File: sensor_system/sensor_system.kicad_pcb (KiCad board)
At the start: 2 copper layers, 49 parts, among them J2 Solar_panels, Q1 SBC817, Q2 MJD45H11, SW1 SW_DPDT_x2, U1 TLC555xD, U2 XC6206PxxxMR, U3 MCP73833, U4 module_bme280_alt, U5 ESP32-DEVKIT-V1, U7 TPS63002

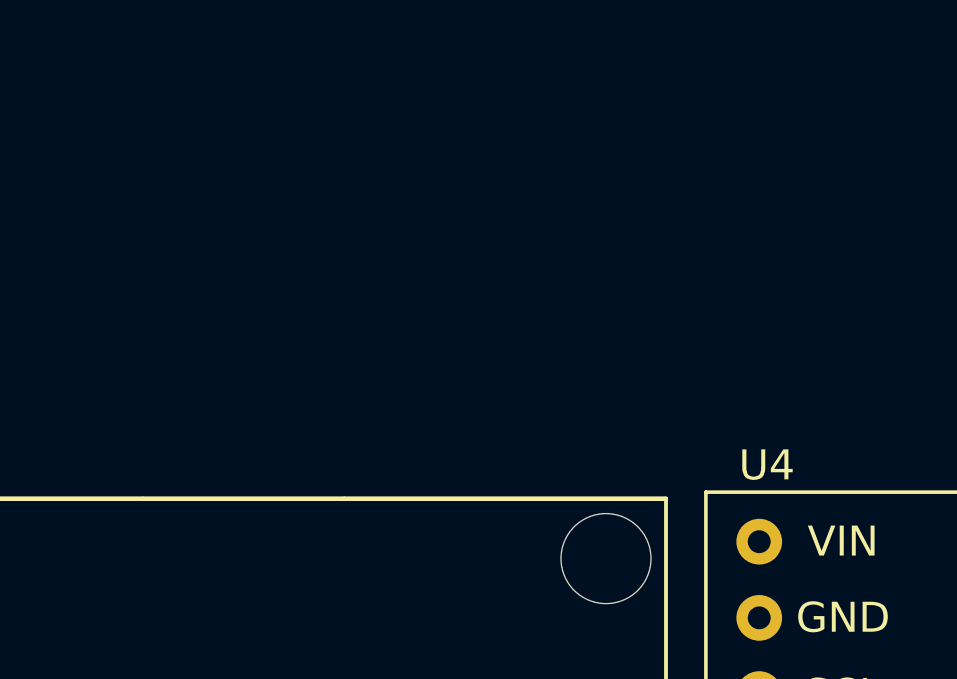
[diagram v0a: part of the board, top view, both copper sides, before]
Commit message: Izveidots footprint magnetiskajam konetoram
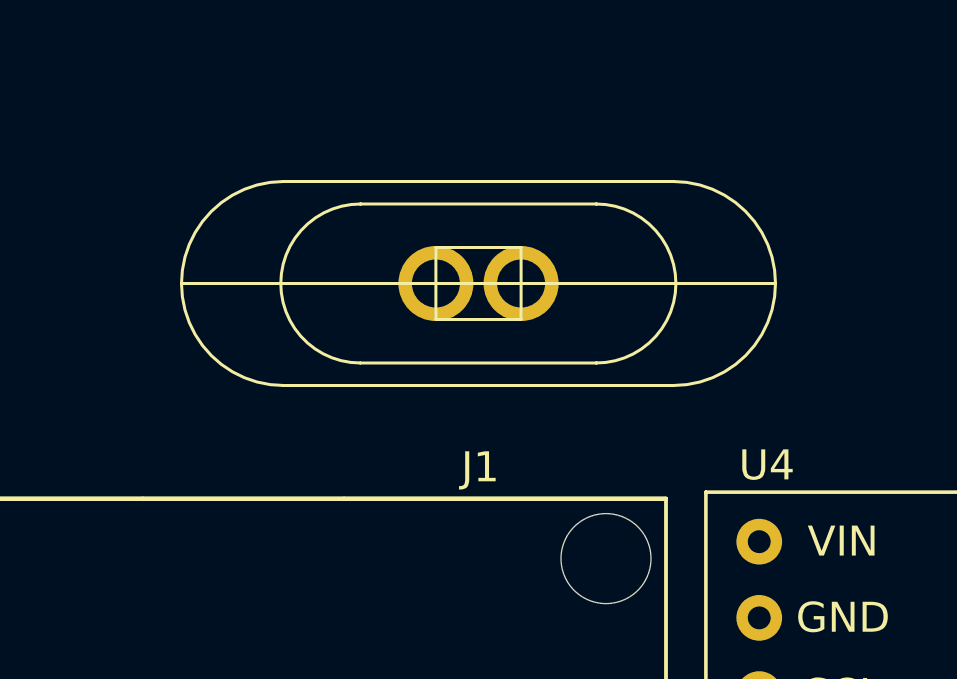
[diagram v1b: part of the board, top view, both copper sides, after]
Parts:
- added J1: Magnetic connector, Magnetic connector:Magnetic connector, F.Cu at (53.0, 25.1)
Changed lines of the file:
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@@
     )
+  )
+  (footprint "Magnetic connector:Magnetic connector" (layer "F.Cu")
+    (at 53.02 25.1)
+    (property "Sheetfile" "power_supply.kicad_sch")
+    (property "Sheetname" "power_supply")
+    (property "ki_description" "Generic screw terminal, single row, 01x02, script generated (kicad-library-utils/schlib/autogen/connector/)")
+    (property "ki_keywords" "screw terminal")
+    (attr smd)
+    (fp_text reference "J1" (at 0.06 6.13 unlocked) (layer "F.SilkS")
+        (effects (font (size 1 1) (thickness 0.1)))
+    )
+    (fp_text value "Magnetic connector" (at 0.16 4.46 unlocked) (layer "F.Fab")
+        (effects (font (size 1 1) (thickness 0.15)))
+    )
+    (fp_line (start -6.5 -3.4) (end 6.5 -3.4)
+      (stroke (width 0.1) (type default)) (layer "F.SilkS"))
+    (fp_line (start -6.5 3.4) (end 6.5 3.4)
+      (stroke (width 0.1) (type default)) (layer "F.SilkS"))
+    (fp_line (start -3.94 -2.65) (end 3.94 -2.65)
+      (stroke (width 0.1) (type default)) (layer "F.SilkS"))
+    (fp_line (start -3.94 2.65) (end 3.94 2.65)
+      (stroke (width 0.1) (type default)) (layer "F.SilkS"))
+    (fp_line (start -1.42 -1.2) (end 1.42 -1.2)
+      (stroke (width 0.1) (type default)) (layer "F.SilkS"))
+    (fp_line (start -1.42 0) (end 1.42 0)
+      (stroke (width 0.1) (type default)) (layer "F.SilkS"))
+    (fp_line (start -1.42 1.2) (end -1.42 -1.2)
+      (stroke (width 0.1) (type default)) (layer "F.SilkS"))
+    (fp_line (start -1.42 1.2) (end 1.42 1.2)
+      (stroke (width 0.1) (type default)) (layer "F.SilkS"))
+    (fp_line (start 1.42 -1.2) (end 1.42 1.2)
+      (stroke (width 0.1) (type default)) (layer "F.SilkS"))
+    (fp_line (start 9.9 0) (end -9.9 0)
+      (stroke (width 0.1) (type default)) (layer "F.SilkS"))
+    (fp_arc (start -6.5 3.4) (mid -9.9 0) (end -6.5 -3.4)
+      (stroke (width 0.1) (type default)) (layer "F.SilkS"))
+    (fp_arc (start -3.94 2.65) (mid -6.590019 -0.010038) (end -3.92 -2.65)
+      (stroke (width 0.1) (type default)) (layer "F.SilkS"))
+    (fp_arc (start 3.92 -2.65) (mid 6.580019 0) (end 3.92 2.65)
+      (stroke (width 0.1) (type default)) (layer "F.SilkS"))
+    (fp_arc (start 6.5 -3.4) (mid 9.9 0) (end 6.5 3.4)
+      (stroke (width 0.1) (type default)) (layer "F.SilkS"))
+    (pad "1" thru_hole circle (at 1.42 0) (size 2.5 2.5) (drill 1.6) (layers "*.Cu" "*.Mask")
+      (net 2 "GNDREF") (pinfunction "Pin_1") (pintype "passive"))
+    (pad "2" thru_hole circle (at -1.42 0) (size 2.5 2.5) (drill 1.6) (layers "*.Cu" "*.Mask")
+      (net 13 "Net-(D2-A1)") (pinfunction "Pin_2") (pintype "passive"))
   )
   (footprint "Connector_PinHeader_2.54mm:PinHeader_1x03_P2.54mm_Horizontal" (layer "F.Cu")

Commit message: Iespiedplate v1
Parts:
- J1: moved to B.Cu
- moved U4 167.0 mm to (228.7, 56.7), turned to 90 degrees
- moved D9 160.1 mm to (221.5, 67.0)
- moved R13 160.1 mm to (228.7, 64.7)
- moved J1 98.5 mm to (148.7, 48.6), turned to -90 degrees
- moved C10 97.8 mm to (165.1, 105.5)
- moved D8 97.8 mm to (184.5, 112.2)
- moved BT1 97.8 mm to (169.8, 105.0)
- moved C13 97.8 mm to (183.7, 104.3)
- moved C14 97.8 mm to (183.7, 106.8)
- moved C15 97.8 mm to (183.7, 109.3)
- moved C9 97.8 mm to (171.7, 112.0)
- moved D2 97.8 mm to (185.4, 101.2)
- moved D3 97.8 mm to (178.8, 104.7)
- moved D4 97.8 mm to (178.8, 108.0)
- moved D5 97.8 mm to (158.5, 109.7)
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
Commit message: Disaster in progress
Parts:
- added D10: ON/OFF, LED_SMD:LED_0603_1608Metric, F.Cu at (150.4, 26.3)
- added R14: 470, Resistor_SMD:R_0805_2012Metric, F.Cu at (152.3, 26.1)
- J2: footprint TerminalBlock:TerminalBlock_bornier-2_P5.08mm -> TestPoint:TestPoint_2Pads_Pitch2.54mm_Drill0.8mm
- U4: moved to B.Cu
- moved C15 96.2 mm to (109.6, 48.0), turned to -90 degrees
- moved C13 94.6 mm to (114.0, 40.4)
- moved C14 93.1 mm to (111.6, 48.0), turned to -90 degrees
- moved D8 89.9 mm to (127.4, 42.7), turned to 180 degrees
- moved Q1 89.4 mm to (122.7, 42.1), turned to -90 degrees
- moved R16 87.4 mm to (110.5, 40.6), turned to 180 degrees
- moved U4 86.8 mm to (147.4, 26.2), turned to 0 degrees
- moved C10 86.4 mm to (107.4, 41.3), turned to -90 degrees
- moved L2 86.3 mm to (115.4, 44.1), turned to -90 degrees
- moved U7 84.8 mm to (110.6, 44.2), turned to 180 degrees
- moved Q2 84.4 mm to (119.1, 35.6), turned to 180 degrees
- moved BT1 84.0 mm to (131.8, 30.2)
- moved TH1 82.7 mm to (135.1, 32.1), turned to 180 degrees
- moved D4 80.8 mm to (141.3, 36.5)
- moved C9 78.3 mm to (164.8, 34.0), turned to -90 degrees
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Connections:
- net +3V0 renamed 3V
- C6 pad 1: /power_supply/5V -> 3V3
- C8 pad 1: /power_supply/5V -> 3V3
- U2 pad 3: /power_supply/5V -> 3V3
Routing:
- net (no net): track 0.00 -> 109.1 mm
- net Net-(D1-A): track 0.00 -> 68.4 mm
- net Soil: track 0.00 -> 39.3 mm, vias 0 -> 1
- net 3V: track 0.00 -> 39.3 mm
- net 3V3: track 0.00 -> 24.2 mm, vias 0 -> 2
- net Net-(U1-THR): track 0.00 -> 14.3 mm, vias 0 -> 3
- net /power_supply/5V: track 0.00 -> 13.9 mm
- net Net-(Q2-E): track 0.00 -> 12.2 mm
- net Net-(D10-A): track 0.00 -> 8.68 mm
- net Net-(U1-Q): track 0.00 -> 7.99 mm
- net Net-(D8-A): track 0.00 -> 7.33 mm
- net Net-(U1-DIS): track 0.00 -> 6.09 mm
- net Net-(U7-EN): track 0.00 -> 5.97 mm
- net Net-(Q2-B): track 0.00 -> 5.02 mm
- net Net-(D8-K): track 0.00 -> 4.88 mm
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
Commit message: Board V1 with one mistake
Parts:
- J1: moved to F.Cu
- U5: moved to B.Cu
- moved C9 30.2 mm to (137.4, 47.0), turned to 180 degrees
- moved C15 26.1 mm to (126.8, 28.4), turned to 90 degrees
- moved C14 23.6 mm to (124.8, 28.4), turned to 90 degrees
- moved R9 23.4 mm to (108.0, 47.4), turned to 180 degrees
- moved C10 22.5 mm to (129.1, 35.1), turned to 90 degrees
- moved D8 19.9 mm to (107.5, 43.5), turned to 90 degrees
- moved U7 19.4 mm to (125.8, 32.2), turned to 0 degrees
- moved R10 19.1 mm to (111.5, 46.7)
- moved SW1 18.2 mm to (125.5, 47.2)
- moved J2 17.5 mm to (149.8, 51.0), turned to 180 degrees
- moved D2 16.5 mm to (158.9, 38.5)
- moved R16 16.2 mm to (126.0, 35.9), turned to 0 degrees
- moved R12 14.7 mm to (114.0, 46.7), turned to 90 degrees
- moved D5 14.4 mm to (147.4, 36.2), turned to 0 degrees
- moved BT1 13.3 mm to (128.0, 42.9), turned to 180 degrees
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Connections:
- BT1 pad 2: GNDREF -> Earth
- C10 pad 2: GNDREF -> Earth
- C13 pad 2: GNDREF -> Earth
- C14 pad 2: GNDREF -> Earth
- C15 pad 2: GNDREF -> Earth
- C9 pad 2: GNDREF -> Earth
- D2 pad 2: GNDREF -> Earth
- J1 pad 1: GNDREF -> Earth
- J2 pad 1: GNDREF -> Earth
- Q1 pad 2: GNDREF -> Earth
- R11 pad 2: GNDREF -> Earth
- R14 pad 1: GNDREF -> Earth
- R8 pad 1: GNDREF -> Earth
- TH1 pad 2: GNDREF -> Earth
- U3 pad 5: GNDREF -> Earth
- U5 pad 19: Net-(D9-A) -> unconnected-(U5-D34-Pad19)
- U5 pad 5: unconnected-(U5-D4-Pad5) -> Net-(D9-A)
- U7 pad 11: GNDREF -> Earth
- U7 pad 3: GNDREF -> Earth
- U7 pad 9: GNDREF -> Earth
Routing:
- net Earth: track 0.00 -> 148.2 mm, vias 0 -> 8
- net (no net): track 109.1 -> 0.00 mm
- net SCL: track 0.00 -> 59.2 mm
- net SDA: track 0.00 -> 49.2 mm
- net Net-(D10-A): track 8.68 -> 47.4 mm, vias 0 -> 2
- net Net-(D9-A): track 0.00 -> 37.2 mm, vias 0 -> 1
- net Net-(D3-K): track 0.00 -> 31.0 mm
- net Net-(D2-A1): track 0.00 -> 18.9 mm
- net Net-(U3-STAT2): track 0.00 -> 14.9 mm
- net Net-(U3-STAT1): track 0.00 -> 14.8 mm
- net 3V3: track 24.2 -> 12.0 mm, vias 2 -> 3
- net Net-(U3-PG): track 0.00 -> 11.8 mm
- net Net-(BT1-+): track 0.00 -> 11.3 mm
- net Net-(Q2-E): track 12.2 -> 21.4 mm
- net Net-(U3-THERM): track 0.00 -> 6.11 mm
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- added copper zone on B.Cu, net 3V3
- added copper zone on F.Cu, net Earth
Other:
- board outline added: 137.1 x 28.5 mm

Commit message: Borad v1
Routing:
- net Earth: track 148.2 -> 142.7 mm, vias 8 -> 7
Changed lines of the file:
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@@
   (via (at 123.45 45.4) (size 0.8) (drill 0.4) (layers "F.Cu" "B.Cu") (free) (net 3))
   (via (at 106.7 40.35) (size 0.8) (drill 0.4) (layers "F.Cu" "B.Cu") (net 3))
-  (via (at 137.1 27.6) (size 0.8) (drill 0.4) (layers "F.Cu" "B.Cu") (free) (net 3))
   (via (at 108.25 30.7) (size 0.8) (drill 0.4) (layers "F.Cu" "B.Cu") (free) (net 3))
   (segment (start 152.65 40) (end 150.75 38.1) (width 0.7) (layer "B.Cu") (net 3))
-  (segment (start 133.06 26.61) (end 133.9 27.45) (width 0.7) (layer "B.Cu") (net 3))
   (segment (start 108.25 27.9) (end 108.25 30.7) (width 1) (layer "B.Cu") (net 3))
   (segment (start 106.7 40.35) (end 106.75 40.4) (width 1) (layer "B.Cu") (net 3))
   (segment (start 123.1 48.8) (end 122.75 48.45) (width 1) (layer "B.Cu") (net 3))
   (segment (start 154.75 40) (end 152.65 40) (width 0.7) (layer "B.Cu") (net 3))
-  (segment (start 136.95 27.45) (end 137.1 27.6) (width 0.7) (layer "B.Cu") (net 3))
   (segment (start 122.75 48.45) (end 122.75 46.1) (width 1) (layer "B.Cu") (net 3))
   (segment (start 106.75 40.4) (end 106.7 40.45) (width 1) (layer "B.Cu") (net 3))
   (segment (start 122.75 46.1) (end 123.45 45.4) (width 1) (layer "B.Cu") (net 3))
-  (segment (start 133.9 27.45) (end 136.95 27.45) (width 0.7) (layer "B.Cu") (net 3))
   (segment (start 150.75 38.1) (end 150.75 36.45) (width 0.7) (layer "B.Cu") (net 3))
   (segment (start 106.75 36.8) (end 106.7 40.35) (width 1) (layer "B.Cu") (net 3))
-  (segment (start 133.06 25.55) (end 133.06 26.61) (width 0.7) (layer "B.Cu") (net 3))
   (segment (start 97.3875 45.825) (end 97.4 45.85) (width 0.5) (layer "F.Cu") (net 4))
   (segment (start 97.3875 43.9625) (end 97.525 43.825) (width 0.5) (layer "F.Cu") (net 4))
@@
   (segment (start 102.5125 40.325) (end 102.5125 38.725) (width 0.5) (layer "B.Cu") (net 5))
   (segment (start 102.5125 38.725) (end 103.7125 37.525) (width 0.5) (layer "B.Cu") (net 5))
-  (segment (start 135.6 26.6) (end 135.6 25.55) (width 0.7) (layer "F.Cu") (net 6))
   (segment (start 124.85 29.225) (end 126.85 29.225) (width 0.6) (layer "F.Cu") (net 6))
   (segment (start 127.25 30.35) (end 127.25 31.23) (width 0.4) (layer "F.Cu") (net 6))
@@
   (segment (start 126.85 29.95) (end 127.25 30.35) (width 0.4) (layer "F.Cu") (net 6))
   (segment (start 124.45 30.25) (end 124.85 29.85) (width 0.4) (layer "F.Cu") (net 6))
-  (segment (start 127.625 29.225) (end 129.25 27.6) (width 0.7) (layer "F.Cu") (net 6))
-  (segment (start 129.25 27.6) (end 134.6 27.6) (width 0.7) (layer "F.Cu") (net 6))
+  (segment (start 133.525 29.225) (end 135.6 27.15) (width 0.7) (layer "F.Cu") (net 6))
+  (segment (start 135.6 27.15) (end 135.6 25.55) (width 0.7) (layer "F.Cu") (net 6))
+  (segment (start 126.85 29.225) (end 133.525 29.225) (width 0.7) (layer "F.Cu") (net 6))
   (segment (start 124.45 30.25) (end 124.45 31.225) (width 0.4) (layer "F.Cu") (net 6))
-  (segment (start 126.85 29.225) (end 127.625 29.225) (width 0.7) (layer "F.Cu") (net 6))
   (segment (start 126.85 29.225) (end 126.85 29.95) (width 0.4) (layer "F.Cu") (net 6))
-  (segment (start 134.6 27.6) (end 135.6 26.6) (width 0.7) (layer "F.Cu") (net 6))
   (segment (start 105.455 34.9125) (end 105.0175 35.35) (width 0.5) (layer "F.Cu") (net 7))
   (segment (start 105.455 34.9125) (end 106.8125 34.9125) (width 0.5) (layer "F.Cu") (net 7))

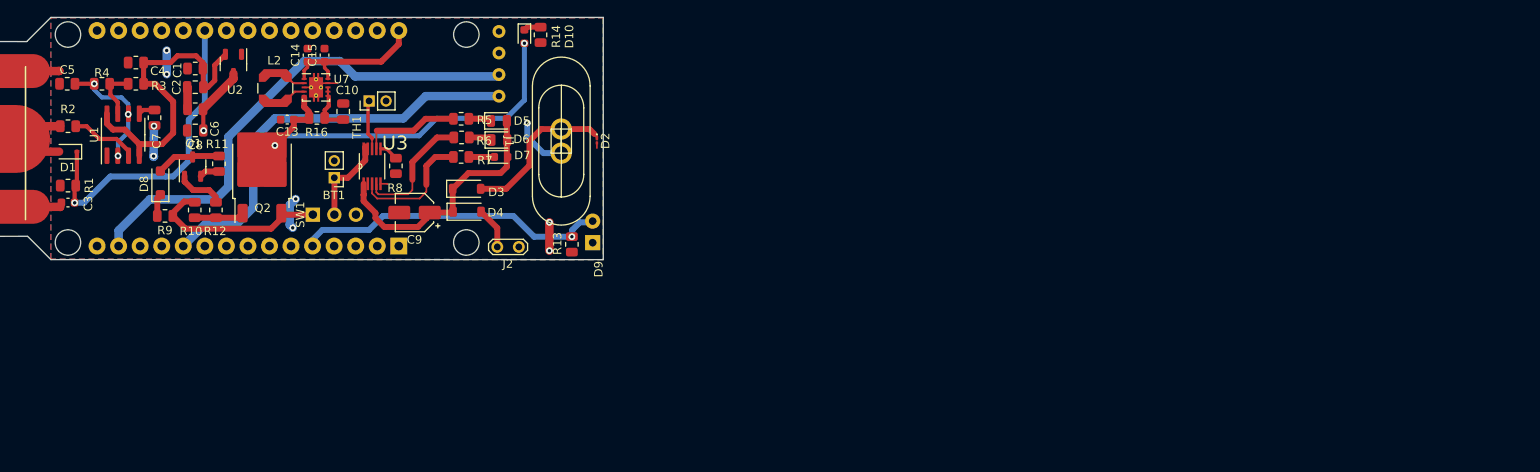
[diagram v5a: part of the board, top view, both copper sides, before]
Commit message: BME280 schematic fix
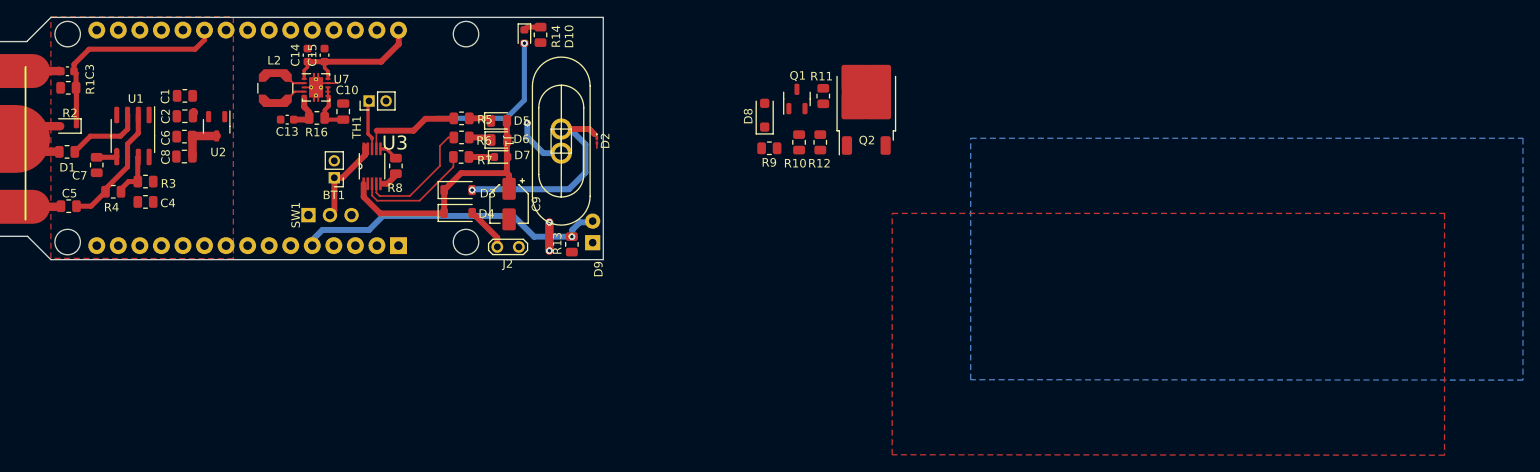
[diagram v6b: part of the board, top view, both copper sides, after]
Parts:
- removed U4: module_bme280_alt, usini_sensors:module_bme280_alt
- moved Q1 71.7 mm to (182.5, 33.6)
- moved R10 71.7 mm to (182.8, 38.7)
- moved R12 71.7 mm to (185.3, 38.7)
- moved R9 71.7 mm to (179.3, 39.4)
- moved D8 71.7 mm to (178.7, 35.5)
- moved Q2 71.7 mm to (190.7, 34.1)
- moved R11 71.7 mm to (185.6, 33.3)
- moved C4 16.5 mm to (105.8, 45.8)
- moved C3 15.5 mm to (96.5, 30.4)
- moved C5 14.4 mm to (96.7, 46.2)
- moved R4 12.8 mm to (102.0, 44.5)
- moved R3 11.6 mm to (105.8, 43.4)
- moved R1 11.5 mm to (96.7, 32.3)
- moved C9 11.2 mm to (148.6, 46.0), turned to -90 degrees
- moved C7 8.80 mm to (100.0, 41.4)
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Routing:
- net SCL: track 59.2 -> 0.00 mm
- net SDA: track 49.2 -> 0.00 mm
- net 3V: track 39.3 -> 0.16 mm
- net Net-(D10-A): track 47.4 -> 21.5 mm, vias 2 -> 1
- net Net-(Q2-E): track 21.4 -> 0.07 mm
- net Earth: track 142.7 -> 128.6 mm, vias 7 -> 1
- net Soil: track 37.8 -> 25.1 mm, vias 1 -> 0
- net Net-(D8-A): track 7.47 -> 0.00 mm
- net Net-(D2-A1): track 18.9 -> 25.9 mm, vias 0 -> 1
- net Net-(Q2-B): track 5.87 -> 0.00 mm
- net Net-(Q1-C): track 5.07 -> 0.00 mm
- net 3V3: track 12.0 -> 8.48 mm, vias 3 -> 2
- net Net-(D8-K): track 2.14 -> 0.00 mm
- net Net-(U1-CV): track 1.98 -> 3.17 mm
- net Net-(U1-Q): track 7.99 -> 9.02 mm
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- added copper zone on F.Cu, net 3V

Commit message: Board V2
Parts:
- added ?: , , F.Cu at (143.7, 32.4)
- added C11: 0u1, Capacitor_SMD:C_0805_2012Metric, F.Cu at (153.1, 25.9)
- added C12: 0u1, Capacitor_SMD:C_0805_2012Metric, F.Cu at (148.7, 29.2)
- added R15: 4k7, Resistor_SMD:R_0805_2012Metric, F.Cu at (136.7, 28.4)
- added R17: 4k7, Resistor_SMD:R_0805_2012Metric, F.Cu at (133.0, 28.4)
- added U4: BME280, Package_LGA:Bosch_LGA-8_2.5x2.5mm_P0.65mm_ClockwisePinNumbering, F.Cu at (148.7, 26.5)
- J1: moved to B.Cu
- moved Q2 67.6 mm to (123.1, 31.8), turned to 180 degrees
- moved R11 65.6 mm to (120.2, 38.4), turned to 90 degrees
- moved Q1 59.0 mm to (123.7, 38.2), turned to -90 degrees
- moved R12 57.5 mm to (127.8, 37.1), turned to 180 degrees
- moved D8 55.7 mm to (123.4, 42.4), turned to 180 degrees
- moved R10 55.0 mm to (127.8, 39.7), turned to 0 degrees
- moved R9 51.6 mm to (127.8, 42.4)
- moved C15 24.8 mm to (111.1, 47.6), turned to 180 degrees
- moved C14 21.7 mm to (114.5, 47.6), turned to 0 degrees
- moved C10 20.4 mm to (109.8, 41.7), turned to -90 degrees
- moved U7 17.8 mm to (113.0, 44.5), turned to 180 degrees
- moved C3 15.5 mm to (96.6, 45.8)
- moved R16 14.1 mm to (112.8, 41.0), turned to 180 degrees
- moved C4 13.9 mm to (107.6, 32.0), turned to -90 degrees
- moved C5 13.6 mm to (97.0, 32.7)
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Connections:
- U5 pad 19: unconnected-(U5-D34-Pad19) -> Net-(D9-A)
- U5 pad 21: Soil -> unconnected-(U5-D32-Pad21)
- U5 pad 28: unconnected-(U5-D13-Pad28) -> Soil
- U5 pad 5: Net-(D9-A) -> unconnected-(U5-D4-Pad5)
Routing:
- net Net-(D10-A): track 21.5 -> 54.4 mm, vias 1 -> 2
- net Net-(Q2-E): track 0.07 -> 25.9 mm
- net SDA: track 0.00 -> 22.2 mm
- net SCL: track 0.00 -> 14.4 mm
- net Net-(D2-A1): track 25.9 -> 12.0 mm, vias 1 -> 0
- net Net-(BT1-+): track 11.2 -> 22.1 mm
- net Net-(D8-A): track 0.00 -> 7.55 mm
- net Net-(D9-A): track 37.2 -> 30.0 mm, vias 1 -> 0
- net Net-(Q2-B): track 0.00 -> 5.87 mm
- net Net-(U3-STAT2): track 14.6 -> 8.92 mm
- net Net-(U3-STAT1): track 14.0 -> 9.22 mm
- net Net-(U3-PG): track 11.8 -> 7.43 mm
- net Soil: track 25.1 -> 21.3 mm
- net Net-(D4-A): track 5.26 -> 8.78 mm
- net Net-(Q1-C): track 0.00 -> 2.30 mm
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
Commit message: Board fix 2.0
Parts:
- removed the ? at (143.7, 32.4)
- removed D2: ESD112B102, Diode_SMD:D_01005_0402Metric
- added ?: , , F.Cu at (97.8, 50.1)
- added ?: , , F.Cu at (97.8, 26.8)
- added ?: , , F.Cu at (141.9, 33.1)
- moved R14 24.5 mm to (147.2, 48.0), turned to 0 degrees
- moved D10 22.0 mm to (147.4, 46.0), turned to 180 degrees
- moved C9 15.5 mm to (151.2, 33.4), turned to 0 degrees
- moved R17 11.9 mm to (144.8, 29.6), turned to -90 degrees
- moved BT1 11.8 mm to (134.8, 34.9), turned to 180 degrees
- moved R11 11.7 mm to (131.9, 38.4)
- moved C14 10.3 mm to (104.5, 45.2), turned to 90 degrees
- moved Q2 10.1 mm to (121.9, 41.8), turned to 90 degrees
- moved D8 8.53 mm to (131.9, 42.5), turned to 90 degrees
- moved SW1 7.80 mm to (132.7, 47.1)
- moved R15 7.35 mm to (143.7, 26.2), turned to 90 degrees
- moved C7 6.59 mm to (112.7, 39.5), turned to 0 degrees
- moved R10 6.56 mm to (127.1, 46.2), turned to 90 degrees
- moved D3 6.44 mm to (151.4, 39.2), turned to 90 degrees
- moved R13 5.78 mm to (154.2, 49.2), turned to -90 degrees
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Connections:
- D9 pad 1: 3V3 -> Net-(D9-K)
- D9 pad 2: Net-(D9-A) -> 3V3
- R13 pad 1: Net-(D9-A) -> Net-(D9-K)
- U5 pad 19: Net-(D9-A) -> Net-(D9-K)
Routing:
- net Net-(D9-K): track 0.00 -> 32.6 mm
- net Net-(D9-A): track 30.0 -> 0.00 mm
- net Net-(Q2-E): track 25.9 -> 7.86 mm
- net Net-(D10-A): track 54.4 -> 41.6 mm
- net Net-(D3-K): track 31.0 -> 21.9 mm
- net 3V3: track 9.03 -> 1.84 mm, vias 7 -> 0
- net Net-(U3-STAT1): track 9.22 -> 2.77 mm
- net 3V: track 0.00 -> 6.24 mm, vias 0 -> 2
- net Net-(D3-A): track 12.0 -> 5.83 mm
- net Net-(Q2-B): track 5.87 -> 12.0 mm
- net Net-(U3-THERM): track 4.09 -> 9.65 mm
- net Net-(U1-THR): track 12.8 -> 18.0 mm, vias 3 -> 0
- net Net-(BT1-+): track 22.1 -> 17.1 mm
- net Net-(U3-STAT2): track 8.92 -> 4.39 mm
- net Net-(U1-DIS): track 5.15 -> 9.51 mm
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- added copper zone on F.Cu, net 3V3
- added copper zone on B.Cu, net Earth
- removed copper zone on B.Cu, net 3V3
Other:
- board size 137.1 x 28.5 mm -> 137.1 x 28.8 mm
